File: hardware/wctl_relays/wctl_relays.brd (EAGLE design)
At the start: 30.5 x 76.8 mm, 38 parts, among them IC1 74LS595D

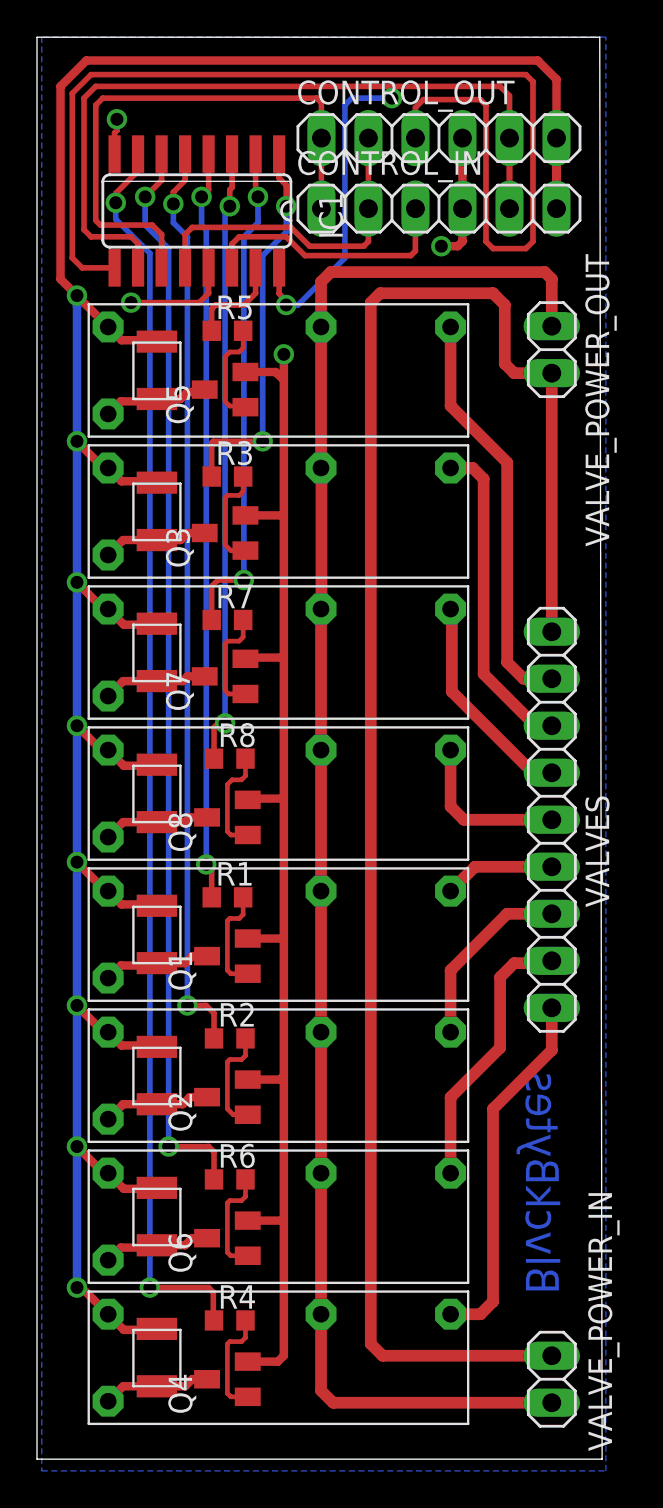
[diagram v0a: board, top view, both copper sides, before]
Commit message: Migrated back to ESP32, updated pins in code and updated hardware, also updated readme
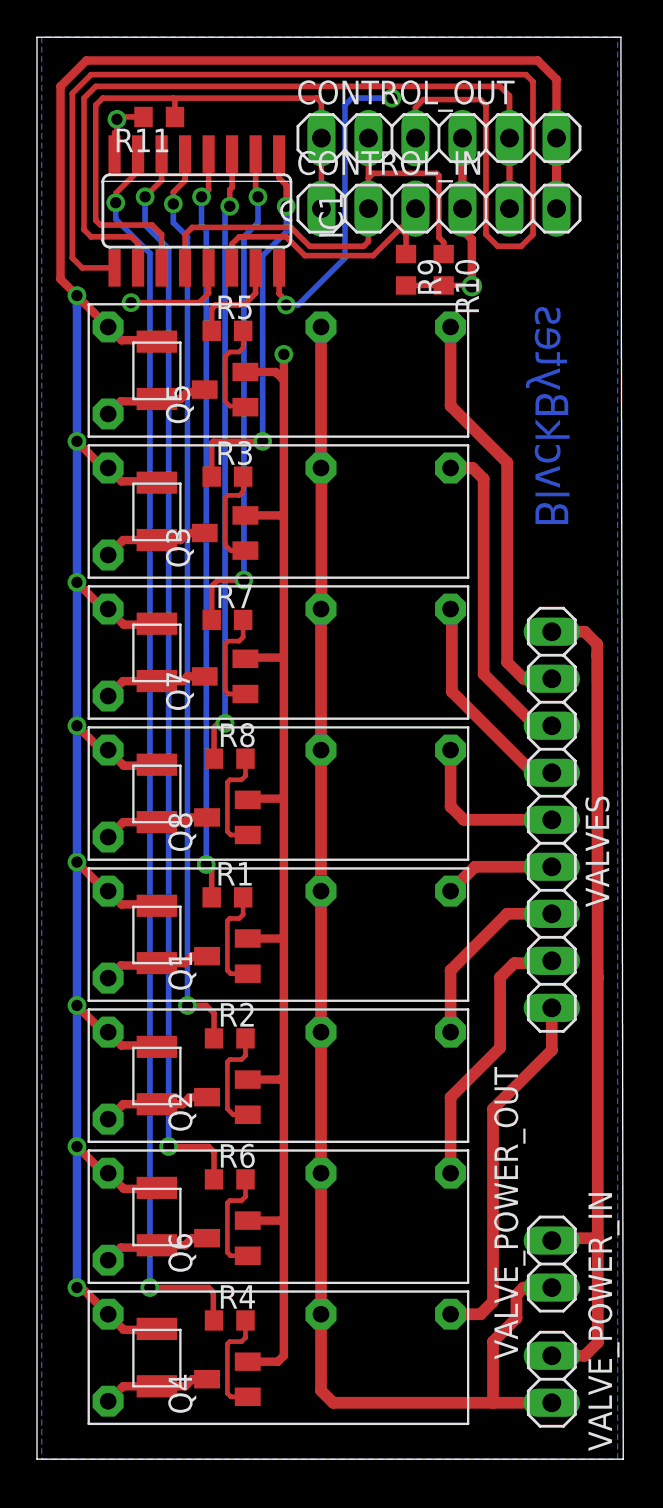
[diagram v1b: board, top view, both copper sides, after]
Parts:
- added R10, R11, R9: 1k, rcl:R0603
- moved VALVE_POWER_OUT 49.4 mm to (60.6, 20.1), turned to 90 degrees
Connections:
- net DATA_IN: now also R9.1
- net GND: now also R10.2, R11.2, R9.2
- net SHIFT: now also R11.1
- net STORE: now also R10.1
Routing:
- net N$10: track 93.9 -> 45.8 mm
- net N$27: track 88.1 -> 78.8 mm
- net STORE: track 18.2 -> 26.5 mm
- net GND: track 85.1 -> 91.5 mm
- net SHIFT: track 30.1 -> 31.1 mm
- net DATA_OUT: track 61.5 -> 60.9 mm
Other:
- board size 30.5 x 76.8 mm -> 31.7 x 76.8 mm
